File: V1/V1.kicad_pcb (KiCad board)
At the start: 2 copper layers, 76.2 x 84.1 mm, 42 parts, among them SW1 SW_Push, U1 ATmega32U4-AU, Y1 16MHz

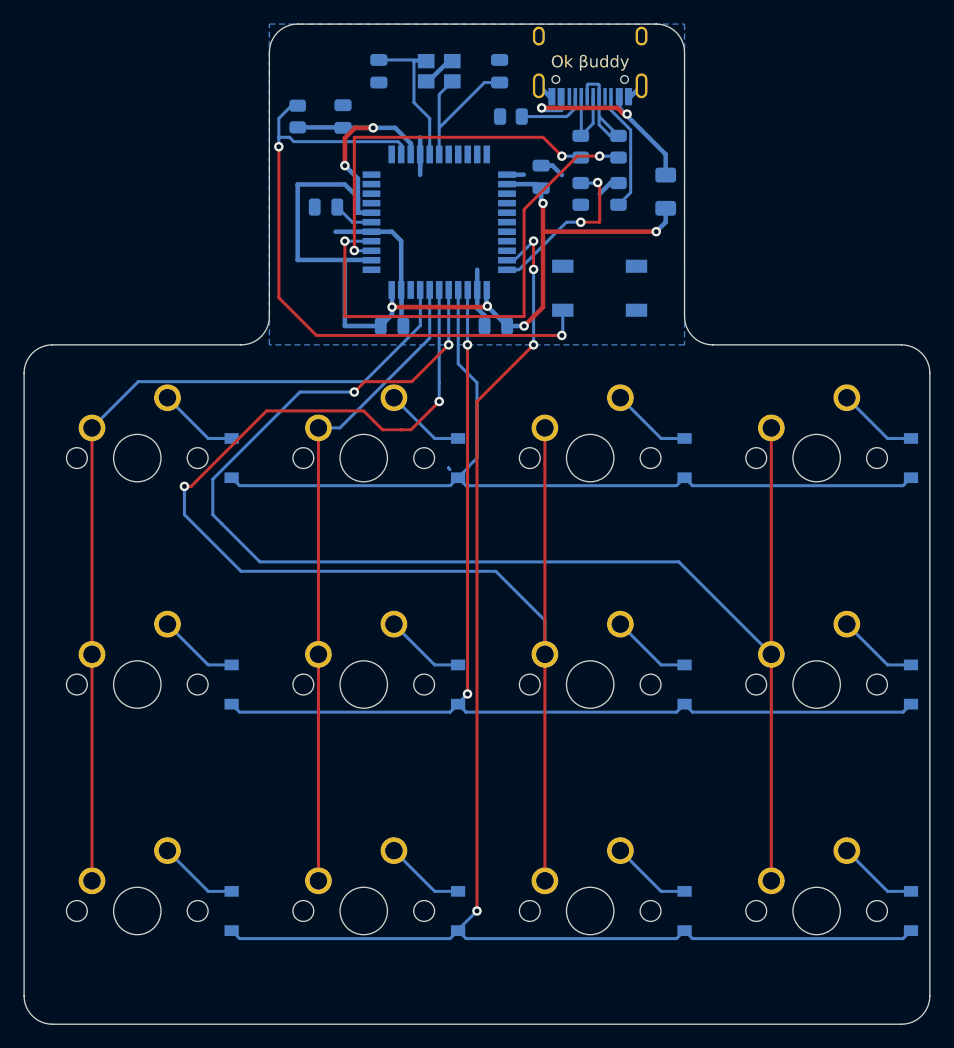
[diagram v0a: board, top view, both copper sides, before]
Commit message: Improved routing
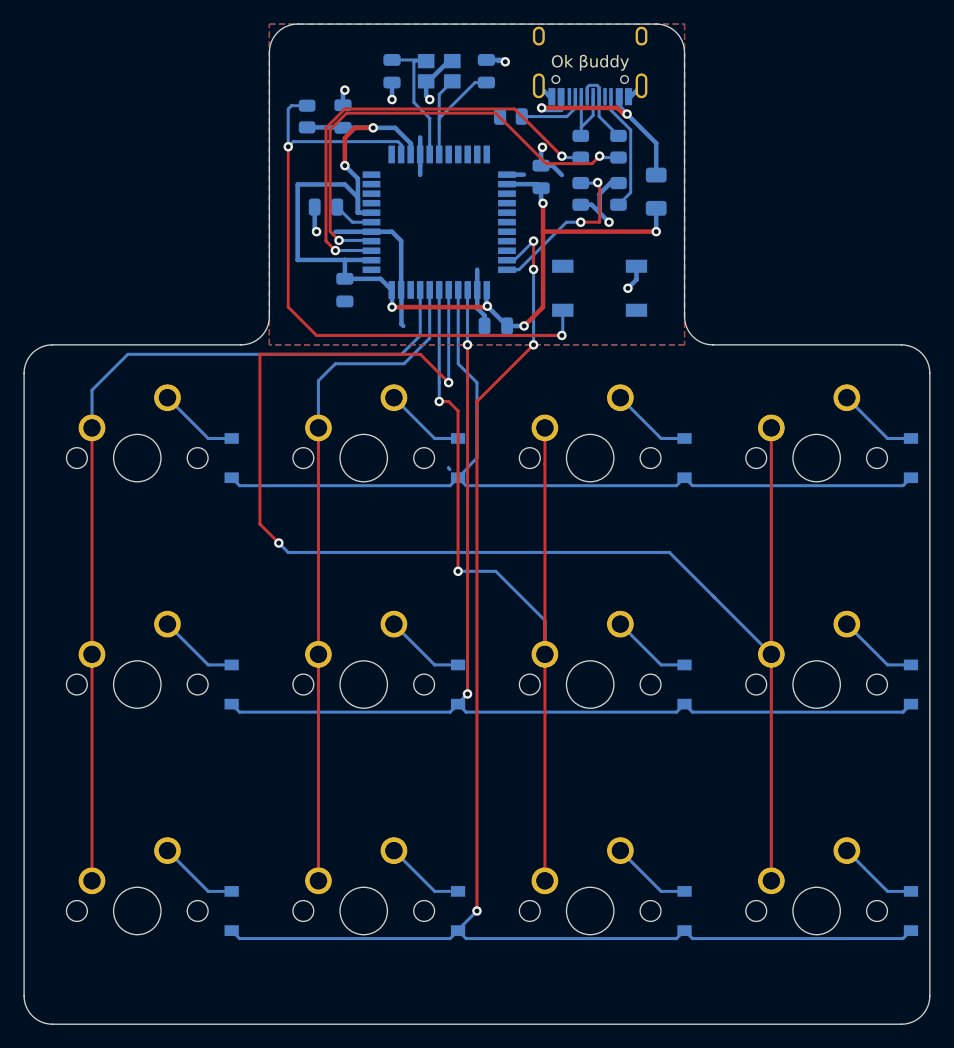
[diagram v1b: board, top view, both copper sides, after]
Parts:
- moved C7 4.99 mm to (82.5, 81.9), turned to 270 degrees
- moved C1 1.11 mm to (94.5, 63.5)
- moved C2 1.11 mm to (86.5, 63.5)
- moved R1 0.79 mm to (79.4, 67.3)
- moved F1 0.79 mm to (108.7, 73.6)
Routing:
- net COL2: track 112.4 -> 74.8 mm
- net GND: track 32.8 -> 49.5 mm, vias 0 -> 8
- net Net-(R3-Pad1): track 30.7 -> 37.5 mm
- net +5V: track 93.4 -> 87.6 mm
- net Net-(R2-Pad1): track 42.5 -> 39.3 mm
- net D+: track 9.67 -> 6.68 mm
- net COL3: track 122.1 -> 124.8 mm
- net COL1: track 54.6 -> 57.0 mm
- net COL0: track 72.4 -> 74.6 mm
- net Net-(C1-Pad1): track 13.4 -> 11.8 mm
- net Net-(C2-Pad1): track 14.2 -> 13.1 mm
- net D-: track 7.17 -> 6.43 mm
- net Net-(R1-Pad2): track 55.8 -> 55.1 mm
- added copper zone on F.Cu, net GND
